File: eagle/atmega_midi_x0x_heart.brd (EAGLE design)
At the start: 100 x 80 mm, 34 parts, among them IC1 TL072P, J11_VCF_CUTOFF 22-23-2021, U1 ATMEGA328P_PDIP

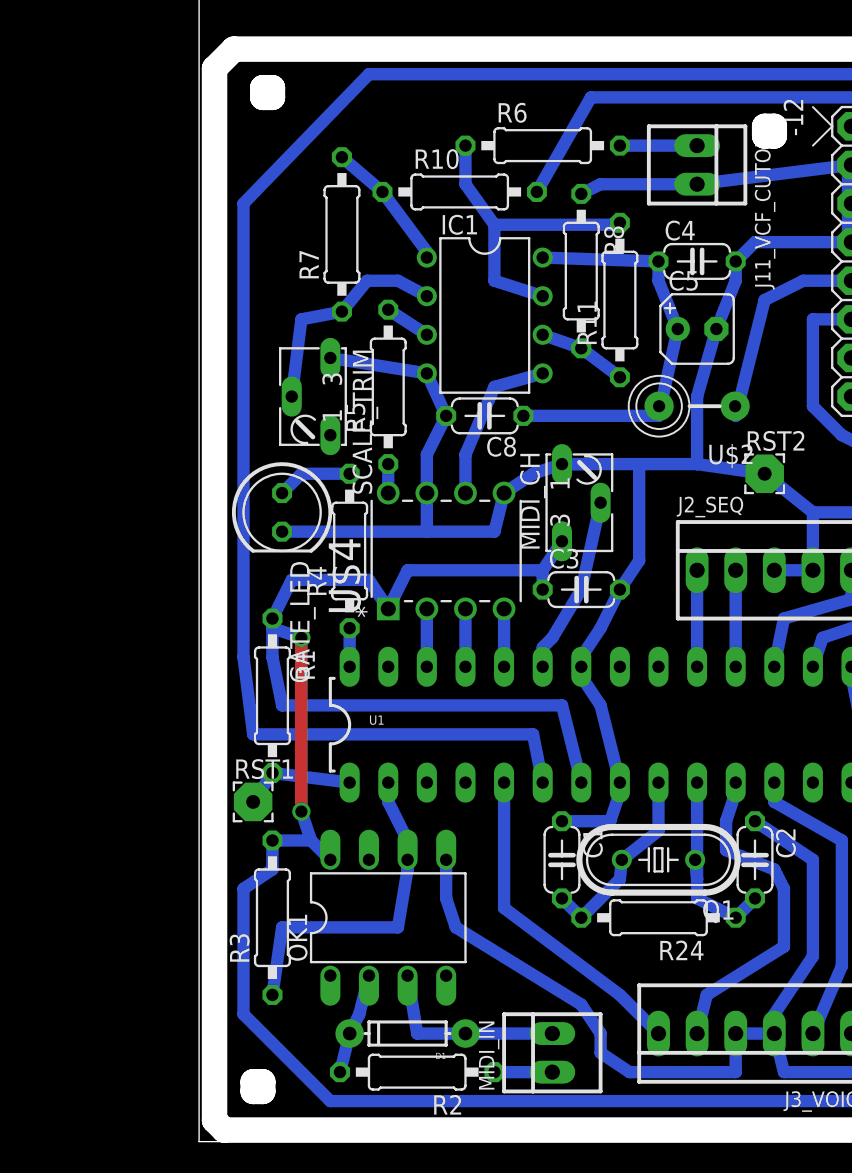
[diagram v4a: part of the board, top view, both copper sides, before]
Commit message: changed to TI precision opamp
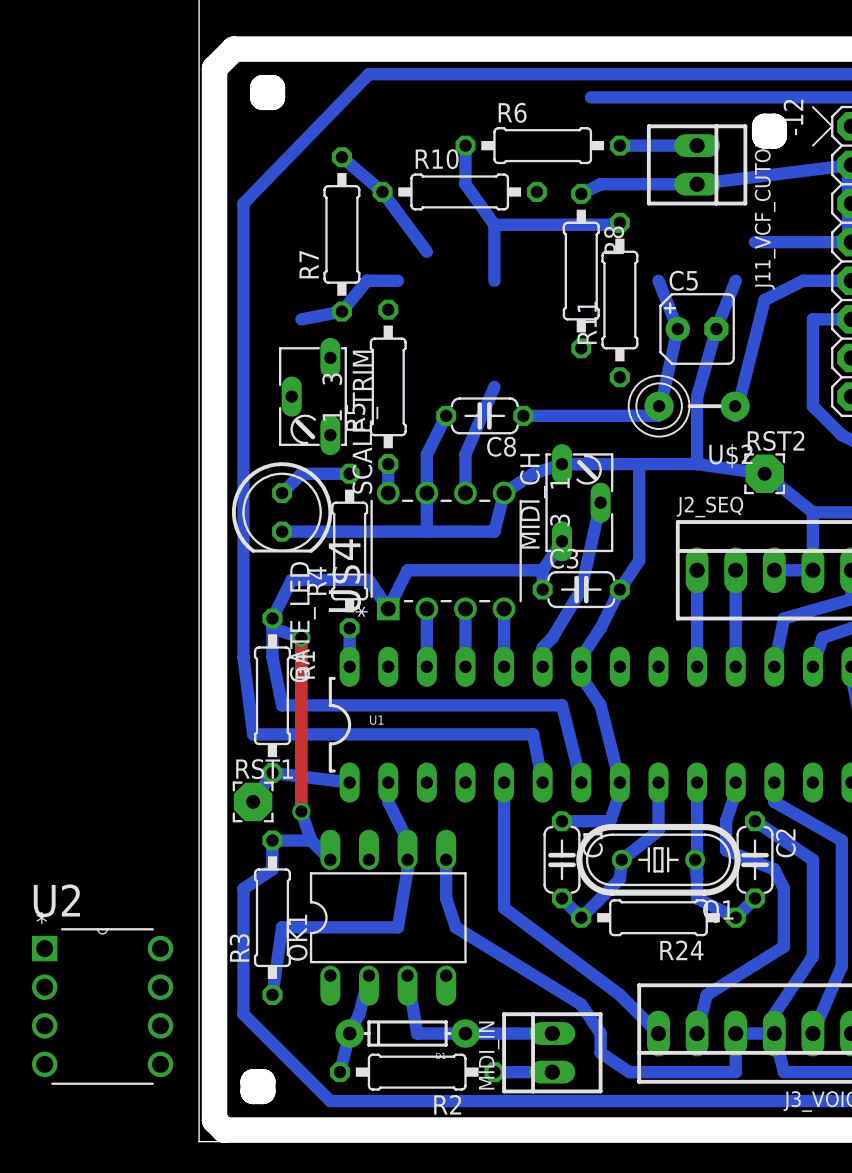
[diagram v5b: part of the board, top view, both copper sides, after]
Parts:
- removed C4: 100n, rcl:C050-024X044
- removed IC1: TL072P, linear:DIL08
- added U2: TLV2372IP, Texas Instruments_By_element14_Batch_1:DIP254P762X508-8
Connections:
- net +12V: now also U2.8; no longer C4.1, IC1.8
- net GND: now also U2.4; no longer C4.2, IC1.4
- net N$12: now also U2.2; no longer IC1.2
- net N$13: now also U2.6; no longer IC1.6
- net N$14: now also U2.5; no longer IC1.5
- net N$15: no longer R10.2
- net N$17: now also U2.7; no longer IC1.7
- net N$27: now also U2.1; no longer IC1.1
- net N$6: now also U2.3; no longer IC1.3
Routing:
- net GND: track 247.2 -> 234.7 mm
- net +12V: track 27.7 -> 18.8 mm
- net N$12: track 14.6 -> 7.37 mm
- net N$15: track 49.6 -> 42.4 mm
- net N$13: track 5.87 -> 0.00 mm
- net N$17: track 21.1 -> 17.8 mm
- net N$14: track 10.7 -> 7.38 mm
- net N$6: track 3.03 -> 0.00 mm
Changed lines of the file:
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@@
 <?xml version="1.0" encoding="utf-8"?>
 <!DOCTYPE eagle SYSTEM "eagle.dtd">
-<eagle version="7.1.0">
+<eagle version="7.2.0">
 <drawing>
 <settings>
@@
 <element name="C2" library="rcl" package="C050-024X044" value="27pF" x="36.576" y="18.542" rot="R270"/>
 <element name="C3" library="rcl" package="C050-024X044" value=".1uF" x="25.146" y="36.322"/>
-<element name="C4" library="rcl" package="C050-024X044" value="100n" x="32.766" y="57.912"/>
 <element name="C5" library="rcl" package="B45181A" value="10u" x="32.766" y="53.467"/>
 <element name="C8" library="rcl" package="C050-024X044" value="100n" x="18.796" y="47.752" rot="R180"/>
 <element name="D1" library="SparkFun-DiscreteSemi" package="DIODE-1N4148" value="" x="13.716" y="7.112" rot="R180"/>
-<element name="IC1" library="linear" package="DIL08" value="TL072P" x="18.796" y="54.356" rot="R270"/>
 <element name="J11_VCF_CUTOFF" library="con-molex" package="22-23-2021" value="22-23-2021" x="32.766" y="64.262" rot="R270">
 <attribute name="OC_NEWARK" value="25C3832" x="32.766" y="64.262" size="1.778" layer="27" rot="R270" display="off"/>
@@
 <element name="GATE_LED" library="led" package="LED5MM" value="" x="5.461" y="41.402" rot="R270"/>
 <element name="R6" library="rcl" package="0207/10" value="100k" x="22.606" y="65.532"/>
+<element name="U2" library="Texas Instruments_By_element14_Batch_1" package="DIP254P762X508-8" value="TLV2372IP" x="-2.54" y="5.08">
+<attribute name="PACKAGE" value="PDIP" x="-2.54" y="5.08" size="1.778" layer="27" display="off"/>
+<attribute name="OC_NEWARK" value="76C7976" x="-2.54" y="5.08" size="1.778" layer="27" display="off"/>
+<attribute name="MPN" value="TLV2372IP" x="-2.54" y="5.08" size="1.778" layer="27" display="off"/>
+<attribute name="SUPPLIER" value="Texas Instruments" x="-2.54" y="5.08" size="1.778" layer="27" display="off"/>
+<attribute name="OC_FARNELL" value="8455031" x="-2.54" y="5.08" size="1.778" layer="27" display="off"/>
+</element>
 </elements>
 <signals>
@@
 <contactref element="U$2" pad="P$2"/>
 <contactref element="C8" pad="1"/>
-<contactref element="C4" pad="1"/>
-<contactref element="IC1" pad="8"/>
-<wire x1="30.226" y1="57.912" x2="22.606" y2="58.166" width="0.8128" layer="16"/>
 <wire x1="30.226" y1="47.752" x2="21.336" y2="47.752" width="0.8128" layer="16"/>
 <wire x1="30.226" y1="47.752" x2="31.496" y2="53.467" width="0.8128" layer="16"/>
 <wire x1="30.266" y1="48.387" x2="30.226" y2="47.752" width="0.8128" layer="16"/>
-<wire x1="30.226" y1="56.642" x2="30.226" y2="57.912" width="0.8128" layer="16"/>
 <wire x1="31.496" y1="53.467" x2="30.226" y2="56.642" width="0.8128" layer="16"/>
+<contactref element="U2" pad="8"/>
+<wire x1="-2.54" y1="12.7" x2="21.336" y2="47.752" width="0" layer="19" extent="1-1"/>
 </signal>
 <signal name="N$2">
@@
 <signal name="N$6">
 <contactref element="R5" pad="2"/>
-<contactref element="IC1" pad="3"/>
-<wire x1="12.446" y1="54.737" x2="14.986" y2="53.086" width="0.8128" layer="16"/>
+<contactref element="U2" pad="3"/>
+<wire x1="-10.16" y1="7.62" x2="12.446" y2="54.737" width="0" layer="19" extent="1-1"/>
 </signal>
 <signal name="N$12">
-<contactref element="SCALE_TRIM" pad="S"/>
 <contactref element="R7" pad="1"/>
-<contactref element="IC1" pad="2"/>
-<wire x1="6.731" y1="54.102" x2="6.096" y2="49.022" width="0.8128" layer="16"/>
 <wire x1="9.398" y1="54.61" x2="6.731" y2="54.102" width="0.8128" layer="16"/>
-<wire x1="13.081" y1="56.642" x2="14.986" y2="55.626" width="0.8128" layer="16"/>
 <wire x1="11.049" y1="56.642" x2="13.081" y2="56.642" width="0.8128" layer="16"/>
 <wire x1="9.398" y1="54.61" x2="11.049" y2="56.642" width="0.8128" layer="16"/>
+<contactref element="SCALE_TRIM" pad="S"/>
+<contactref element="U2" pad="2"/>
+<wire x1="6.096" y1="49.022" x2="6.731" y2="54.102" width="0" layer="19" extent="16-16"/>
+<wire x1="-10.16" y1="10.16" x2="6.096" y2="49.022" width="0" layer="19" extent="1-1"/>
 </signal>
 <signal name="N$13">
+<contactref element="R11" pad="1"/>
+<contactref element="U2" pad="6"/>
 <contactref element="R8" pad="2"/>
-<contactref element="R11" pad="1"/>
-<contactref element="IC1" pad="6"/>
-<wire x1="25.146" y1="52.197" x2="22.606" y2="53.086" width="0.8128" layer="16"/>
-<wire x1="25.146" y1="52.197" x2="27.686" y2="50.292" width="0.8128" layer="16"/>
+<wire x1="25.146" y1="52.197" x2="27.686" y2="50.292" width="0" layer="19" extent="1-1"/>
+<wire x1="-2.54" y1="7.62" x2="27.686" y2="50.292" width="0" layer="19" extent="1-1"/>
 </signal>
 <signal name="N$17">
 <contactref element="R11" pad="2"/>
-<contactref element="IC1" pad="7"/>
-<wire x1="19.431" y1="56.642" x2="22.606" y2="55.626" width="0.8128" layer="16"/>
 <wire x1="19.431" y1="60.325" x2="19.431" y2="56.642" width="0.8128" layer="16"/>
 <wire x1="27.051" y1="60.325" x2="19.431" y2="60.325" width="0.8128" layer="16"/>
@@
 <wire x1="17.526" y1="65.532" x2="17.526" y2="62.992" width="0.8128" layer="16"/>
 <wire x1="17.526" y1="62.992" x2="19.431" y2="60.325" width="0.8128" layer="16"/>
+<contactref element="U2" pad="7"/>
+<wire x1="-2.54" y1="10.16" x2="19.431" y2="56.642" width="0" layer="19" extent="16-16"/>
 </signal>
 <signal name="N$25">
@@
 <signal name="N$14">
 <contactref element="U$4" pad="6"/>
-<contactref element="IC1" pad="5"/>
-<wire x1="19.431" y1="49.657" x2="22.606" y2="50.546" width="0.8128" layer="16"/>
 <wire x1="17.526" y1="45.212" x2="19.431" y2="49.657" width="0.8128" layer="16"/>
 <wire x1="17.526" y1="42.672" x2="17.526" y2="45.212" width="0.8128" layer="16"/>
+<contactref element="U2" pad="5"/>
+<wire x1="-2.54" y1="5.08" x2="17.526" y2="42.672" width="0" layer="19" extent="1-1"/>
 </signal>
 <signal name="N$11">
@@
 <contactref element="R10" pad="1"/>
 <contactref element="R7" pad="2"/>
-<contactref element="IC1" pad="1"/>
-<wire x1="14.986" y1="58.547" x2="14.986" y2="58.166" width="0.8128" layer="16"/>
 <wire x1="12.065" y1="62.484" x2="14.986" y2="58.547" width="0.8128" layer="16"/>
 <wire x1="12.065" y1="62.484" x2="9.398" y2="64.77" width="0.8128" layer="16"/>
+<contactref element="U2" pad="1"/>
+<wire x1="-10.16" y1="12.7" x2="14.986" y2="58.547" width="0" layer="19" extent="16-16"/>
 </signal>
 <signal name="N$15">
 <contactref element="PWR1" pad="13"/>
 <contactref element="PWR1" pad="14"/>
-<contactref element="R10" pad="2"/>
-<wire x1="25.781" y1="68.707" x2="22.225" y2="62.484" width="0.8128" layer="16"/>
 <wire x1="46.101" y1="68.707" x2="25.781" y2="68.707" width="0.8128" layer="16"/>
 <wire x1="47.371" y1="67.437" x2="46.101" y2="68.707" width="0.8128" layer="16"/>
@@
 <contactref element="C5" pad="-"/>
 <contactref element="C8" pad="2"/>
-<contactref element="C4" pad="2"/>
-<contactref element="IC1" pad="4"/>
 <contactref element="J11_VCF_CUTOFF" pad="2"/>
 <contactref element="SCALE_TRIM" pad="E"/>
@@
 <wire x1="26.416" y1="62.992" x2="25.146" y2="62.357" width="0.8128" layer="16"/>
 <wire x1="32.766" y1="62.992" x2="26.416" y2="62.992" width="0.8128" layer="16"/>
-<wire x1="35.306" y1="56.642" x2="35.306" y2="57.912" width="0.8128" layer="16"/>
 <wire x1="34.036" y1="53.467" x2="35.306" y2="56.642" width="0.8128" layer="16"/>
 <wire x1="45.466" y1="64.262" x2="42.926" y2="64.262" width="0.8128" layer="16"/>
@@
 <wire x1="42.926" y1="61.722" x2="45.466" y2="61.722" width="0.8128" layer="16"/>
 <wire x1="42.926" y1="61.722" x2="42.926" y2="64.262" width="0.8128" layer="16"/>
-<wire x1="36.576" y1="59.182" x2="35.306" y2="57.912" width="0.8128" layer="16"/>
 <wire x1="42.926" y1="59.182" x2="36.576" y2="59.182" width="0.8128" layer="16"/>
 <wire x1="42.926" y1="64.262" x2="32.766" y2="62.992" width="0.8128" layer="16"/>
-<wire x1="14.986" y1="50.546" x2="16.256" y2="47.752" width="0.8128" layer="16"/>
-<wire x1="14.986" y1="50.546" x2="8.636" y2="51.562" width="0.8128" layer="16"/>
 <wire x1="14.986" y1="45.212" x2="14.986" y2="42.672" width="0.8128" layer="16"/>
 <wire x1="16.256" y1="47.752" x2="14.986" y2="45.212" width="0.8128" layer="16"/>
@@
 <wire x1="32.766" y1="44.577" x2="37.211" y2="43.942" width="0.8128" layer="16"/>
 <wire x1="40.386" y1="41.402" x2="40.386" y2="37.592" width="0.8128" layer="16"/>
+<contactref element="U2" pad="4"/>
+<wire x1="35.306" y1="56.642" x2="36.576" y2="59.182" width="0" layer="19" extent="16-16"/>
+<wire x1="8.636" y1="51.562" x2="16.256" y2="47.752" width="0" layer="19" extent="1-1"/>
+<wire x1="-10.16" y1="5.08" x2="16.891" y2="14.097" width="0" layer="19" extent="16-16"/>
 </signal>
 <signal name="N$24">

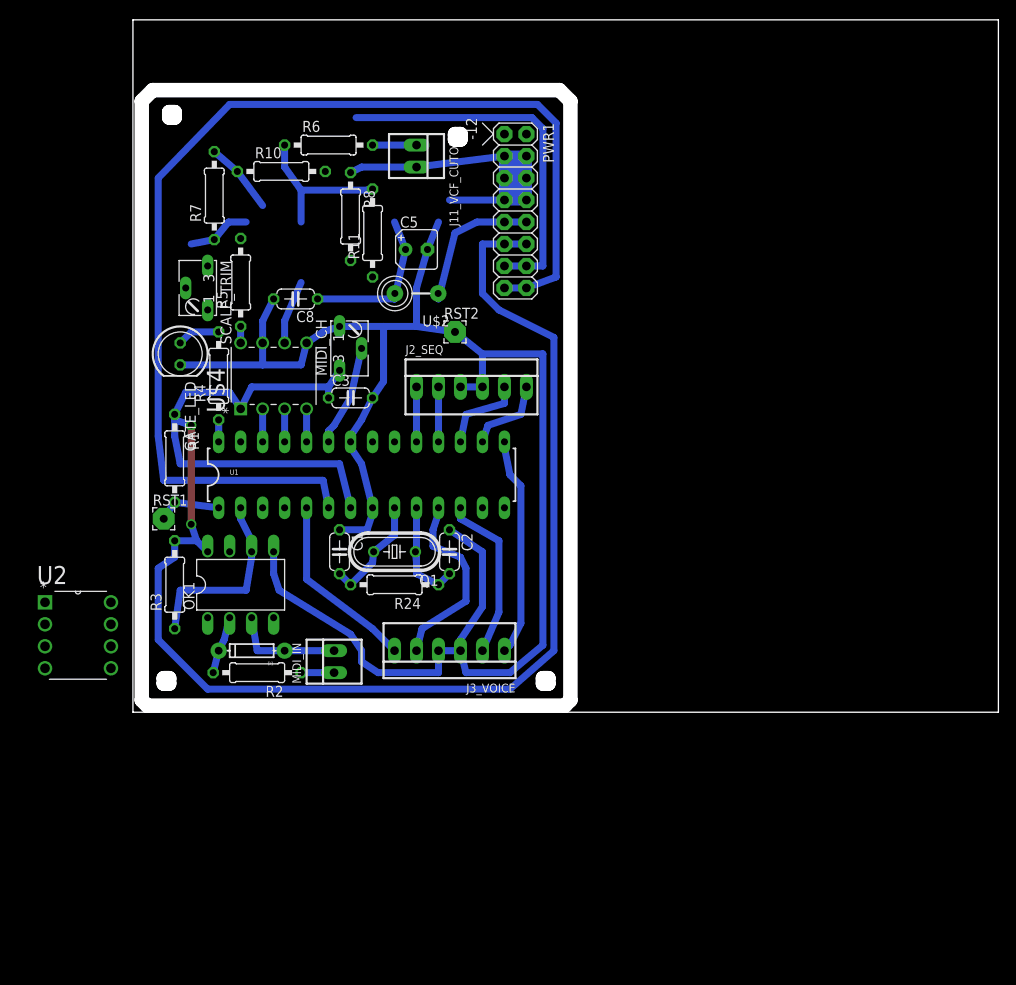
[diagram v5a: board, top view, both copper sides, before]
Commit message: tweaked cutout for better holes
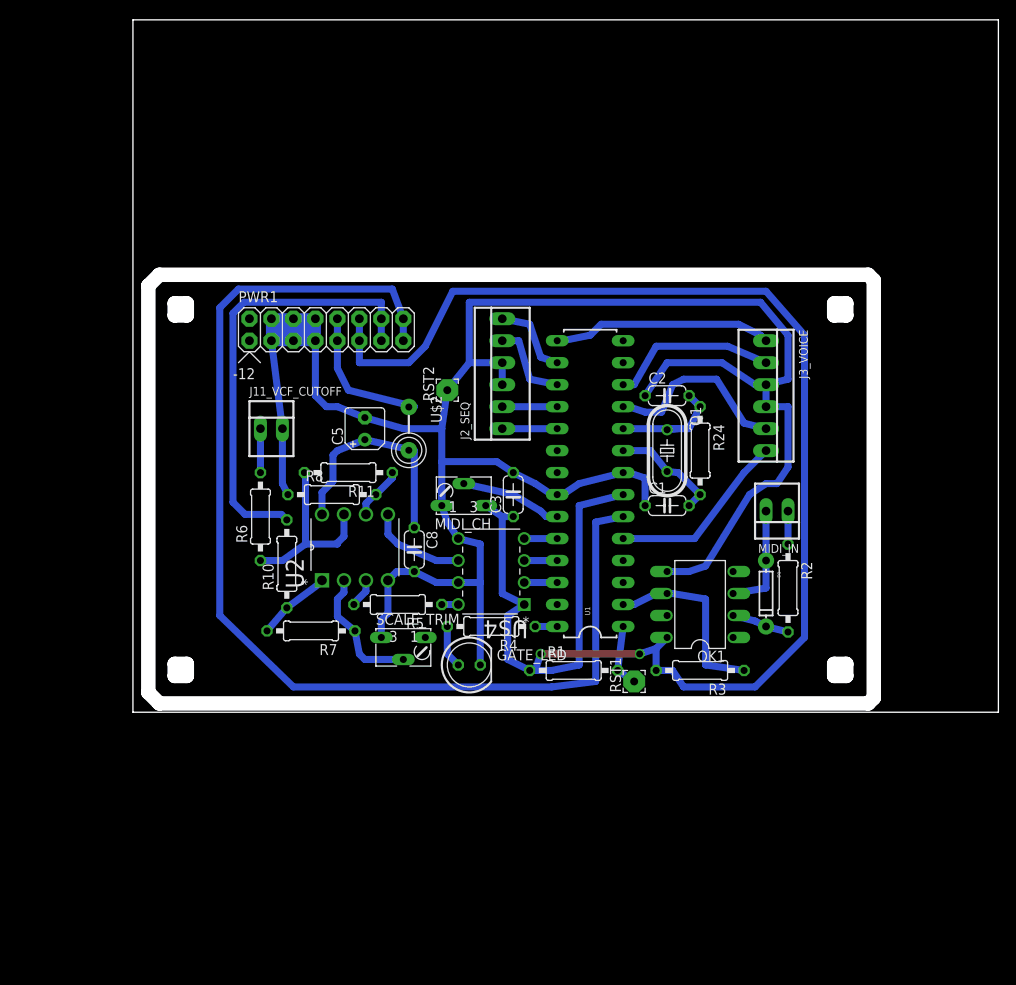
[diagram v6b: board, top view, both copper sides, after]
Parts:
- moved R2 62.1 mm to (75.7, 14.4), turned to 270 degrees
- moved R3 61.5 mm to (65.5, 4.83), turned to 180 degrees
- moved D1 59.8 mm to (73.2, 13.7), turned to 270 degrees
- moved RST1 57.5 mm to (57.9, 3.56), turned to 90 degrees
- moved MIDI_IN 54.1 mm to (74.4, 23.2), turned to 180 degrees
- moved OK1 53.1 mm to (65.5, 12.4), turned to 90 degrees
- moved R1 52.2 mm to (50.9, 4.83), turned to 0 degrees
- moved R7 51.5 mm to (20.6, 9.40), turned to 180 degrees
- moved GATE_LED 49.1 mm to (38.9, 5.46), turned to 0 degrees
- moved J3_VOICE 47.0 mm to (73.2, 36.6), turned to 270 degrees
- moved SCALE_TRIM 46.3 mm to (31.2, 8.64), turned to 0 degrees
- moved R10 45.3 mm to (17.8, 17.1), turned to 90 degrees
- moved R6 43.6 mm to (14.7, 22.6), turned to 90 degrees
- moved R4 42.8 mm to (41.4, 9.91), turned to 180 degrees
- moved R5 41.4 mm to (30.6, 12.4), turned to 180 degrees
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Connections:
- net N$15: now also R10.2
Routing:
- net GND: track 234.7 -> 248.1 mm
- net N$15: track 42.4 -> 51.0 mm
- net +12V: track 18.8 -> 26.9 mm
- net N$12: track 7.37 -> 15.2 mm
- net N$13: track 0.00 -> 6.16 mm
- net N$14: track 7.38 -> 11.3 mm
- net N$17: track 17.8 -> 21.5 mm
- net N$6: track 0.00 -> 3.37 mm
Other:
- outline, holes or cut-outs redrawn
